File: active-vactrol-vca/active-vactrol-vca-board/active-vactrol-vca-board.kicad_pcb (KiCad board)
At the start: 4 copper layers, 19 x 108 mm, 43 parts, among them J1 Thonkiconn_Mono_Audio_Jack, J2 Thonkiconn_Mono_Audio_Jack, J3 Thonkiconn_Mono_Audio_Jack, J4 Thonkiconn_Mono_Audio_Jack, J5 Thonkiconn_Mono_Audio_Jack, J6 Thonkiconn_Mono_Audio_Jack, U1 TL072, U2 TL072, U3 TL072, U4 TL072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

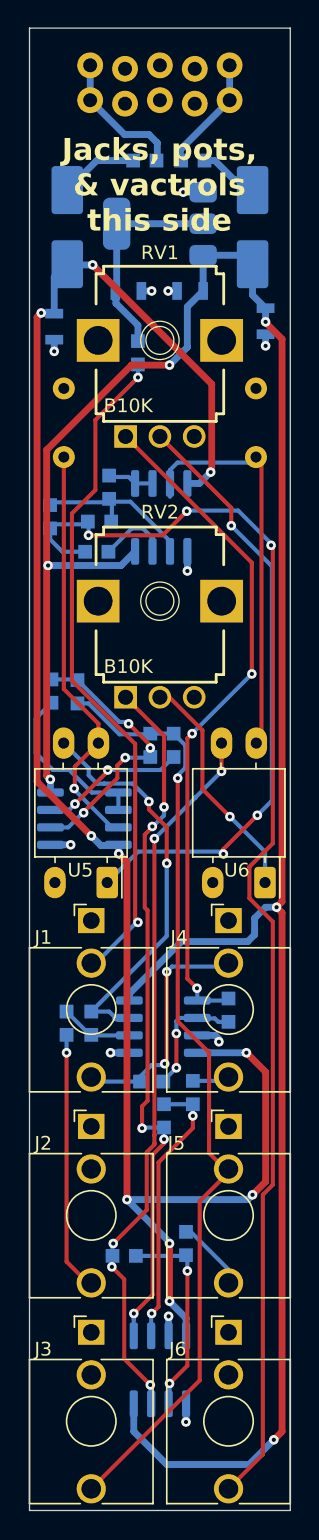
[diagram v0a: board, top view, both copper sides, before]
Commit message: Adds v1.0 of Crustose and updates Vactrol VCA for production. Updates Lichen symbol and footprint library..
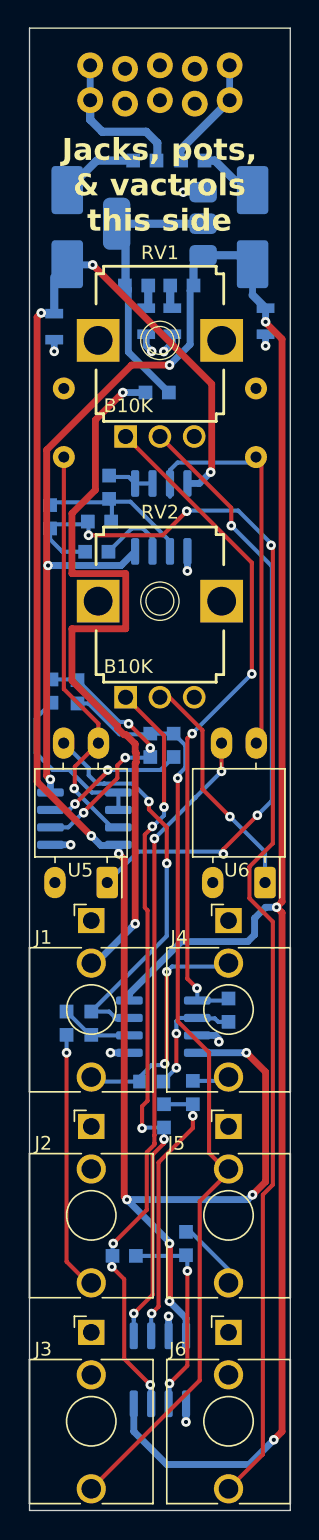
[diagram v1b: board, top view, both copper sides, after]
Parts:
- added R6: 1R, Lichen:R_0603, B.Cu at (111.6, 129.0)
- added R7: 1R, Lichen:R_0603, B.Cu at (108.3, 129.0)
- moved R5 3.22 mm to (109.8, 136.8), turned to 180 degrees
- moved C3 2.56 mm to (110.9, 131.6), turned to 90 degrees
- moved C6 2.56 mm to (109.0, 131.6), turned to 90 degrees
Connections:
- C3 pad 2: +12V -> Net-(C3-Pad2)
- C6 pad 2: +5V -> Net-(C6-Pad2)
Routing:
- net Net-(J1-PadTN): track 49.5 -> 56.4 mm
- net +5V: track 16.6 -> 21.3 mm
- net Net-(C6-Pad2): track 0.00 -> 1.71 mm
- net Net-(C3-Pad2): track 0.00 -> 1.71 mm
- net GND: track 13.5 -> 15.0 mm
- net /-12V_In: track 10.2 -> 11.0 mm

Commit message: Updates Lichen symbols and footprints. Fixes to Crustose and Vactrol VCA. Adds 3D model of the RP2350 dual USB board.
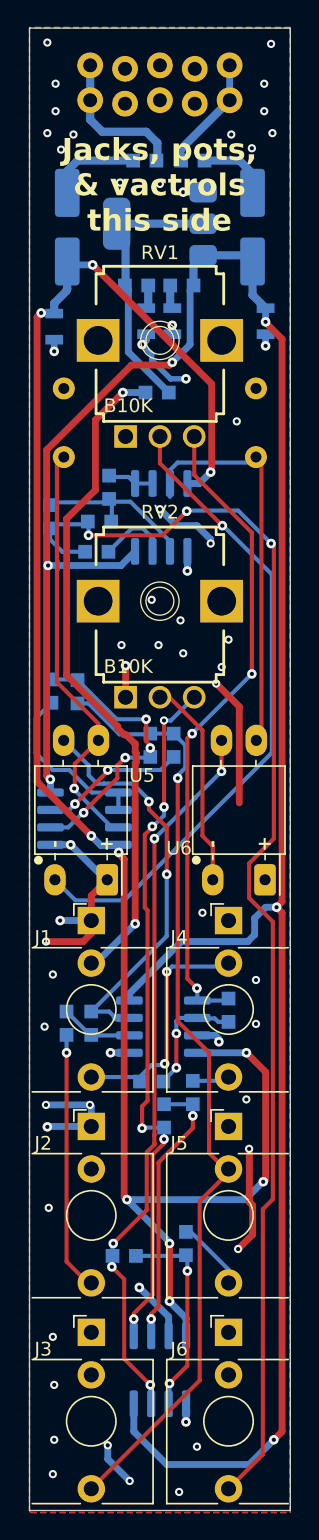
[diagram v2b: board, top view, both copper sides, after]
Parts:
- D1, D2: footprint Diode_SMD:D_SMB_Handsoldering -> Diode_SMD:D_SMA_Handsoldering
- J1, J2, J3: footprint Lichen:Audio_Jack_Thonkiconn_Mono -> Lichen:Audio_Jack_Thonkiconn_Mono_Left_Overhang
- J4, J5, J6: footprint Lichen:Audio_Jack_Thonkiconn_Mono -> Lichen:Audio_Jack_Thonkiconn_Mono_Right_Overhang
- R1, R10, R11, R12, R13, R2, R3, R4, R5: value 100k -> 100k_0603
- R17, R19, R20, R8: value 10k_0603 -> 100k_0603
- R18, R9: value 10k_0603 -> 1k_0603
- moved U5 0.20 mm to (106.2, 172.3)
- moved U6 0.20 mm to (117.7, 172.3)
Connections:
- RV1 pad 1: /Left Gate/L_CV_BUFFERED -> GND
- RV1 pad 3: GND -> /Left Gate/L_CV_BUFFERED
- RV2 pad 1: /Right Gate/R_CV_BUFFERED -> GND
- RV2 pad 3: GND -> /Right Gate/R_CV_BUFFERED
- U5 pad 1: /Left Gate/L_CV_ATTENUATED -> GND
- U5 pad 2: GND -> /Left Gate/L_CV_ATTENUATED
- U6 pad 1: /Right Gate/R_CV_ATTENUATED -> GND
- U6 pad 2: GND -> /Right Gate/R_CV_ATTENUATED
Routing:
- net GND: track 15.0 -> 71.4 mm, vias 11 -> 60
- net Net-(J1-PadTN): track 56.4 -> 48.9 mm
- net /Left Gate/L_CV_ATTENUATED: track 44.7 -> 47.3 mm, vias 3 -> 1
- net /Left Gate/L_CV_BUFFERED: track 49.5 -> 47.4 mm
- net /Right Gate/R_CV_ATTENUATED: track 17.1 -> 15.3 mm, vias 1 -> 0
- net Net-(U2B--): track 20.0 -> 21.0 mm
- net Net-(D1-A): track 5.97 -> 6.88 mm
- net /Right Gate/R_CV_BUFFERED: track 51.1 -> 51.2 mm, vias 5 -> 6
- added copper zone on B.Cu, net GND
- added copper zone on F.Cu, net GND
- removed copper zone on In1.Cu, net GND
- removed copper zone on In2.Cu, net GND
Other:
- copper layers 4 -> 2
- board text added: "Copyright 2026, Lichen Community Systems"
- board text added: "Lichen Latencies v1.1"
- board text removed: "Copyright 2025, Lichen Community Systems"
- board text removed: "Lichen Latencies v1.0"
